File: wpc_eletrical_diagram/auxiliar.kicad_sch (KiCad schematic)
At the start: 8 parts, among them Q3 2N7000, Q4 2N7000

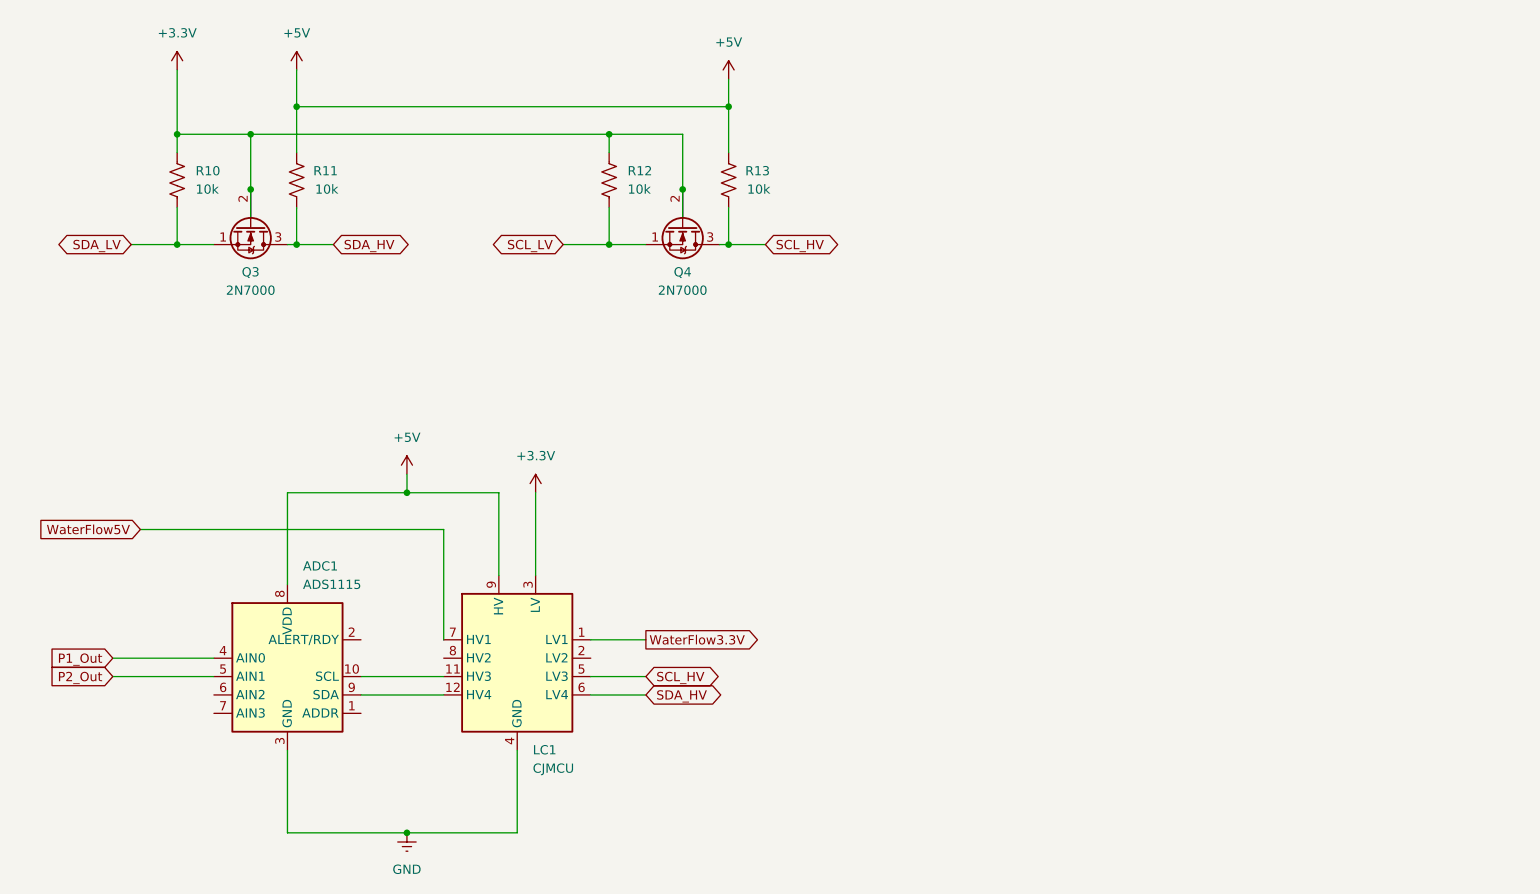
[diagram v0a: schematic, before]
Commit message: eletrical corrections
- schematic correction (sensors, actuation)
- main board correction (resistor values, chottky diodes) (v26)
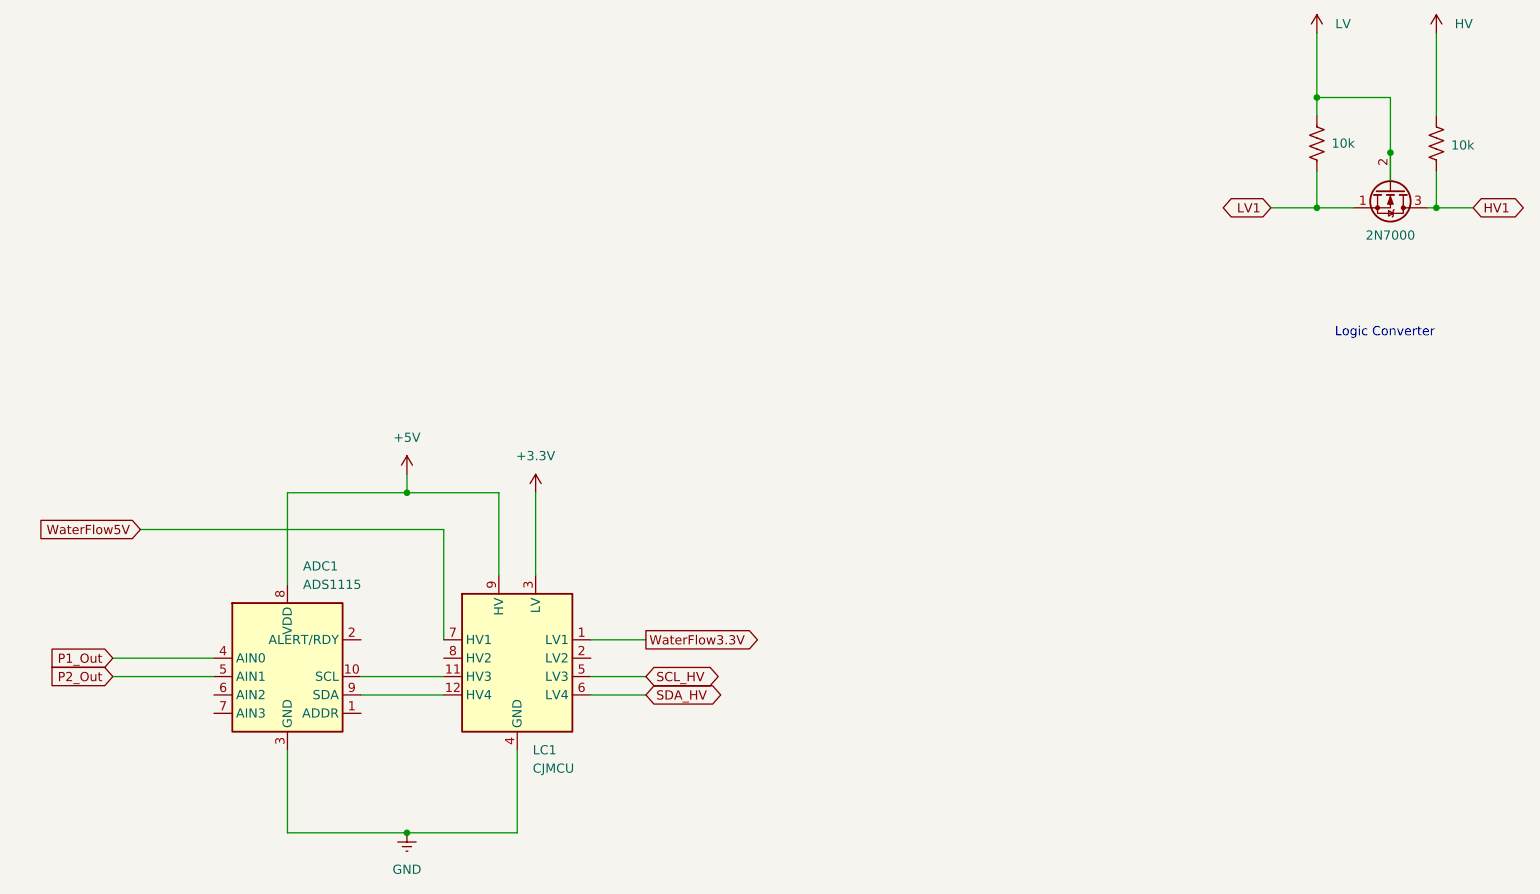
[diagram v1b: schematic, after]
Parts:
- removed Q4: 2N7000, Package_TO_SOT_THT:TO-92_Inline, symbol Transistor_FET:2N7000
- removed R12, R13: 10k, symbol Device:R_US
- renumbered Q3 to Q2
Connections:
- net +3.3V: no longer Q2.2 (G), R10.1
- net +5V: no longer R11.1
- net SDA_HV: no longer Q2.3 (D), R11.2
- net SDA_LV renamed LV1
- new net HV: R11.1
- new net HV1: Q2.3 (D), R11.2
- new net LV: Q2.2 (G), R10.1
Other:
- note added: "Logic Converter"
